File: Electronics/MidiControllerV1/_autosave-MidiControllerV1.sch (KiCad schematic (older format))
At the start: 18 parts

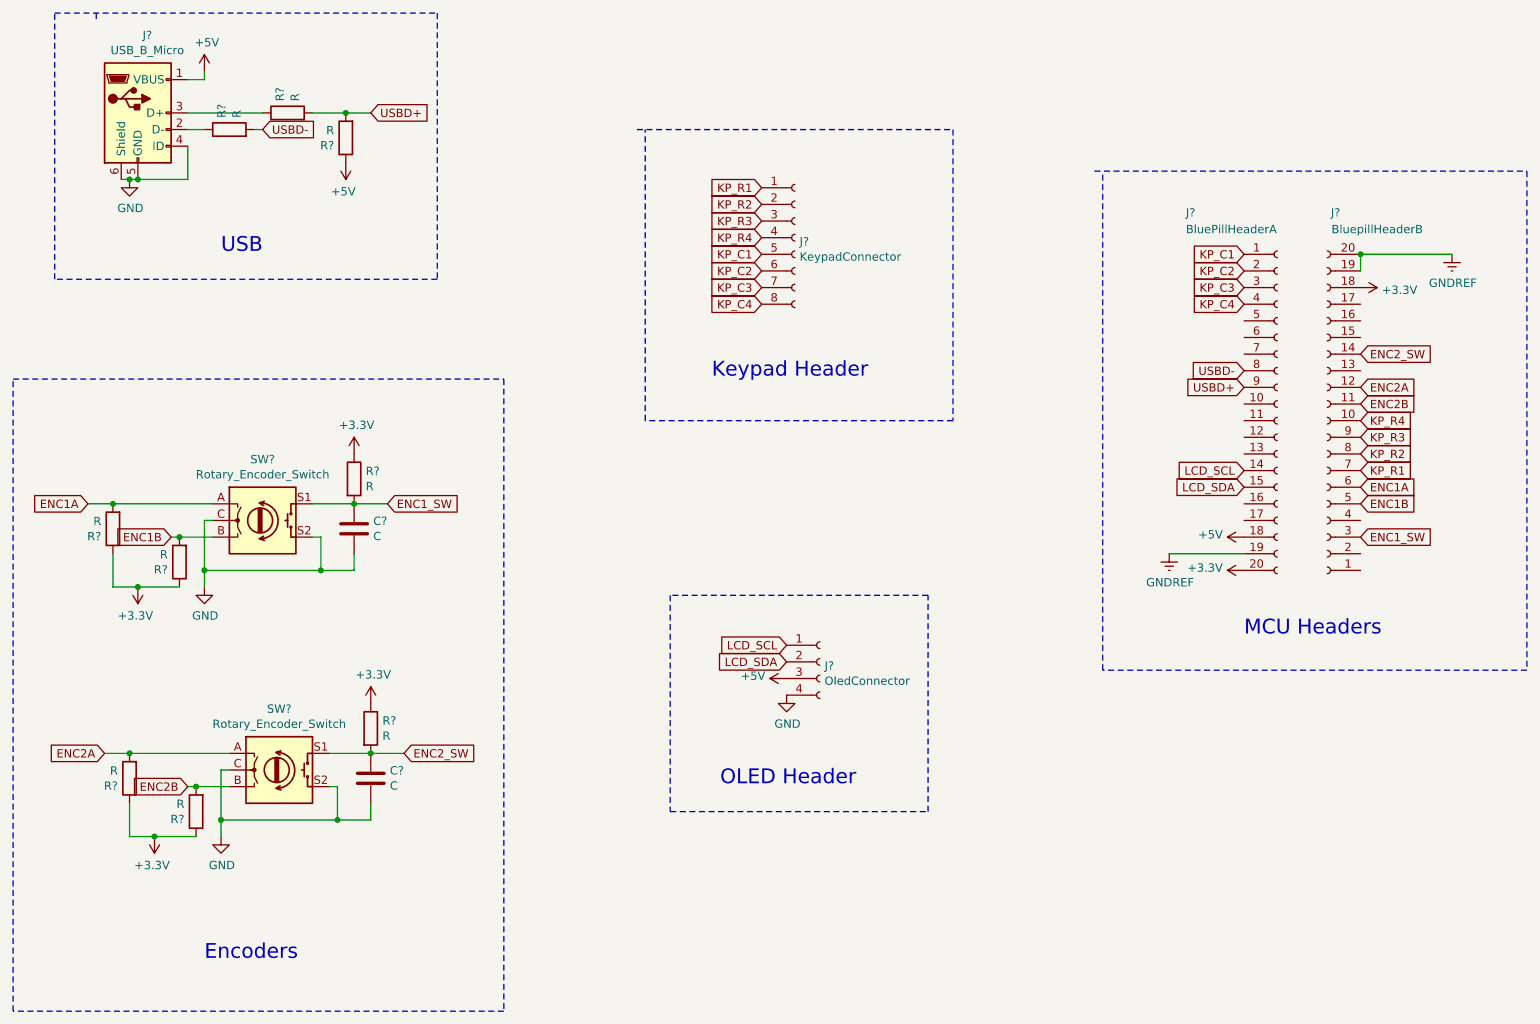
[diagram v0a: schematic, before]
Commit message: Components placed on pcb
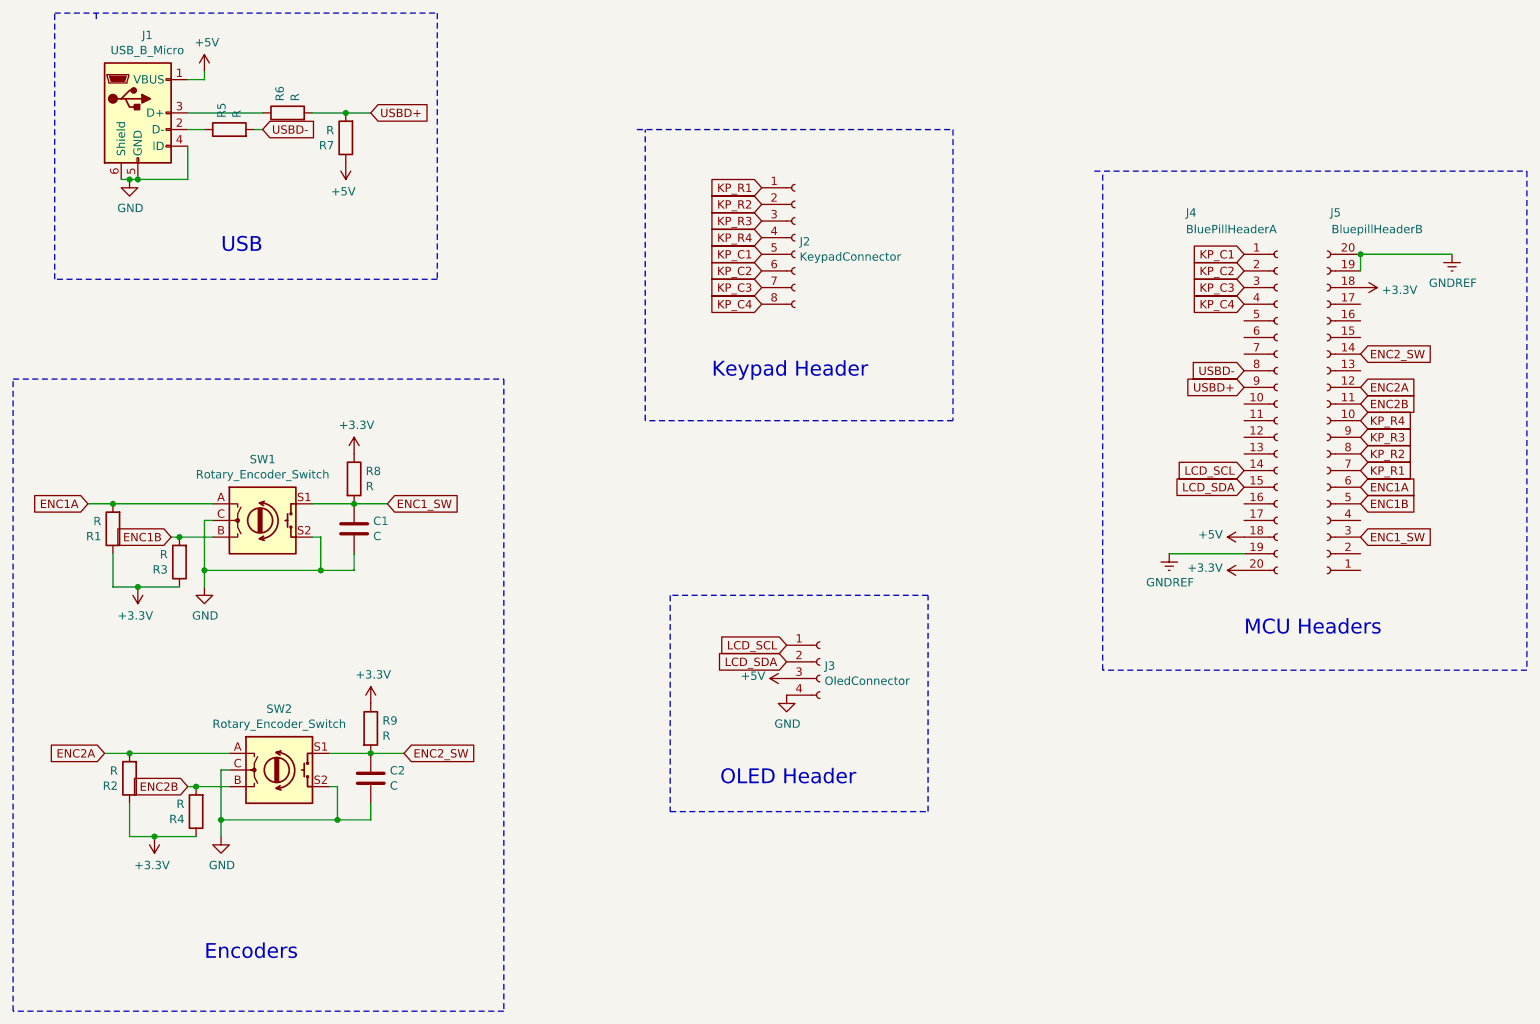
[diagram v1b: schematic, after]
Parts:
- J1: renamed from J?; footprint (none) -> Connector_USB:USB_Micro-B_Molex-105017-0001
- J2: renamed from J?; footprint (none) -> Connector_PinHeader_2.54mm:PinHeader_1x08_P2.54mm_Vertical
- J3: renamed from J?; footprint (none) -> Connector_PinHeader_2.54mm:PinHeader_1x04_P2.54mm_Vertical
- J4, J5: renamed from J?; footprint (none) -> Connector_PinHeader_2.54mm:PinHeader_1x20_P2.54mm_Vertical
- R1, R2, R3, R4, R5, R6, R7, R8, R9: renamed from R?; footprint (none) -> Resistor_SMD:R_1206_3216Metric
- SW1, SW2: renamed from SW?; footprint (none) -> Rotary_Encoder:RotaryEncoder_Alps_EC11E-Switch_Vertical_H20mm
- gave numbers to parts that had none: 2
